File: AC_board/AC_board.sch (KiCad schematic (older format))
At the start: 10 parts, among them J1 1226, J2 7471287, J3 Conn_01x02_Male, J4 7471287, J5 7471287, J6 Conn_01x02_Male, K1 G6B-2214P-US-DC12

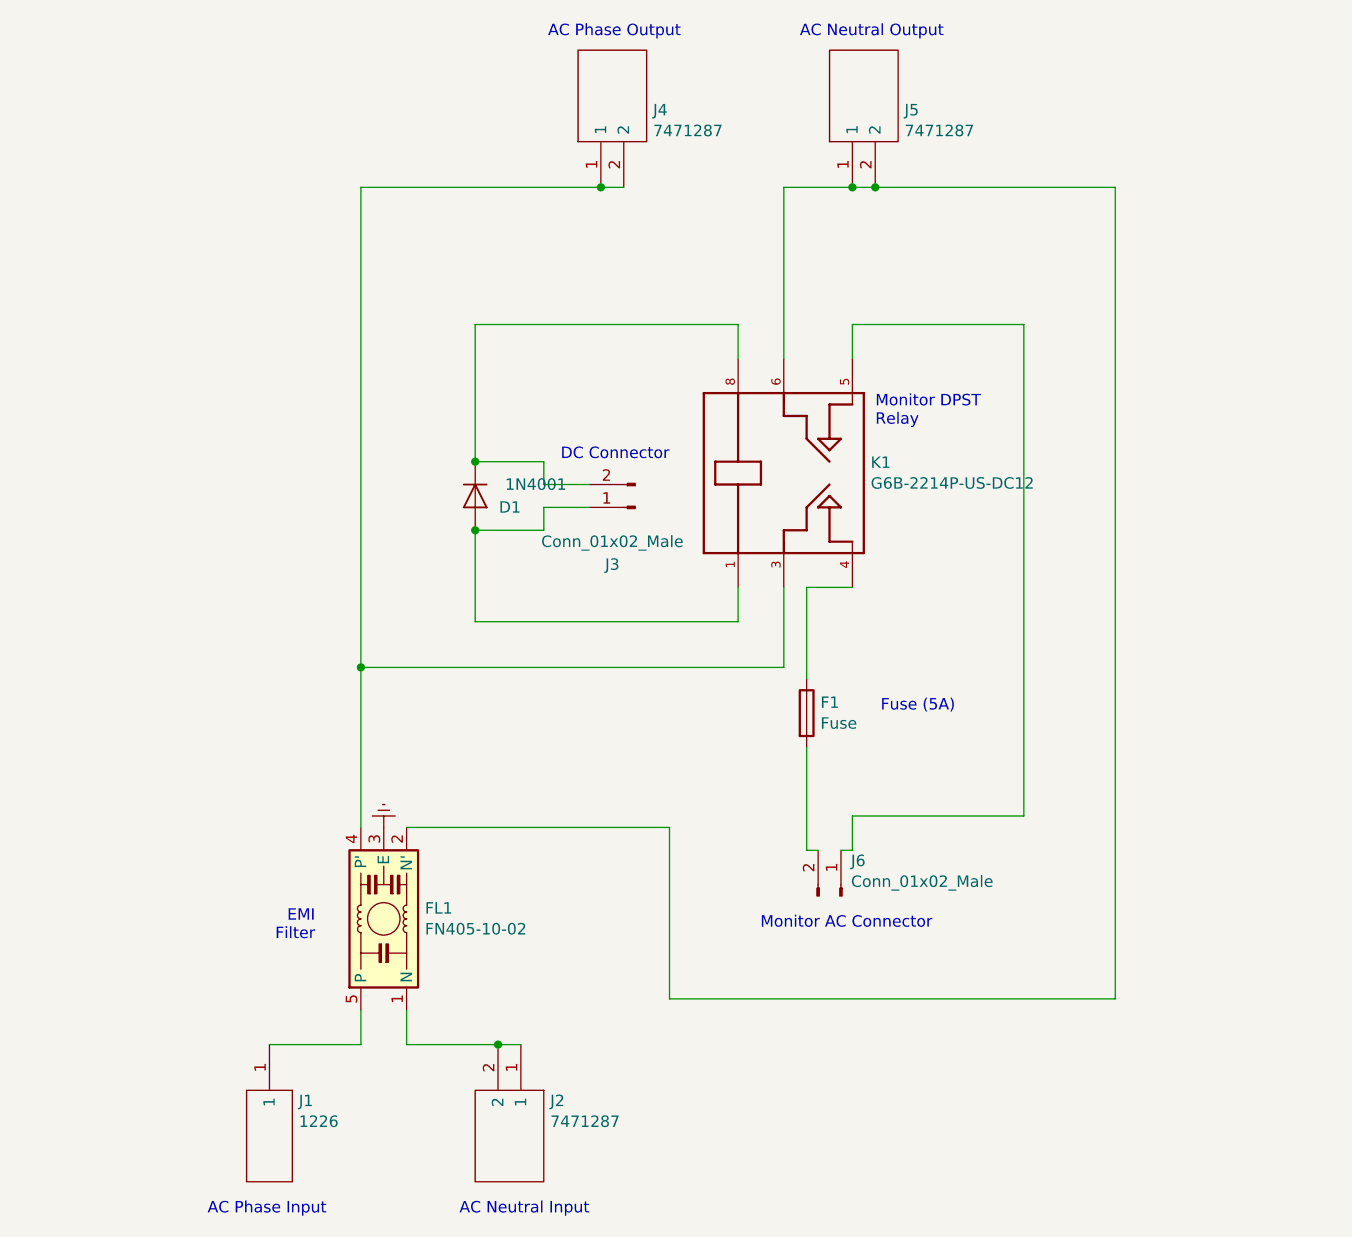
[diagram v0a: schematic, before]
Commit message: Brand new AC and DC boards
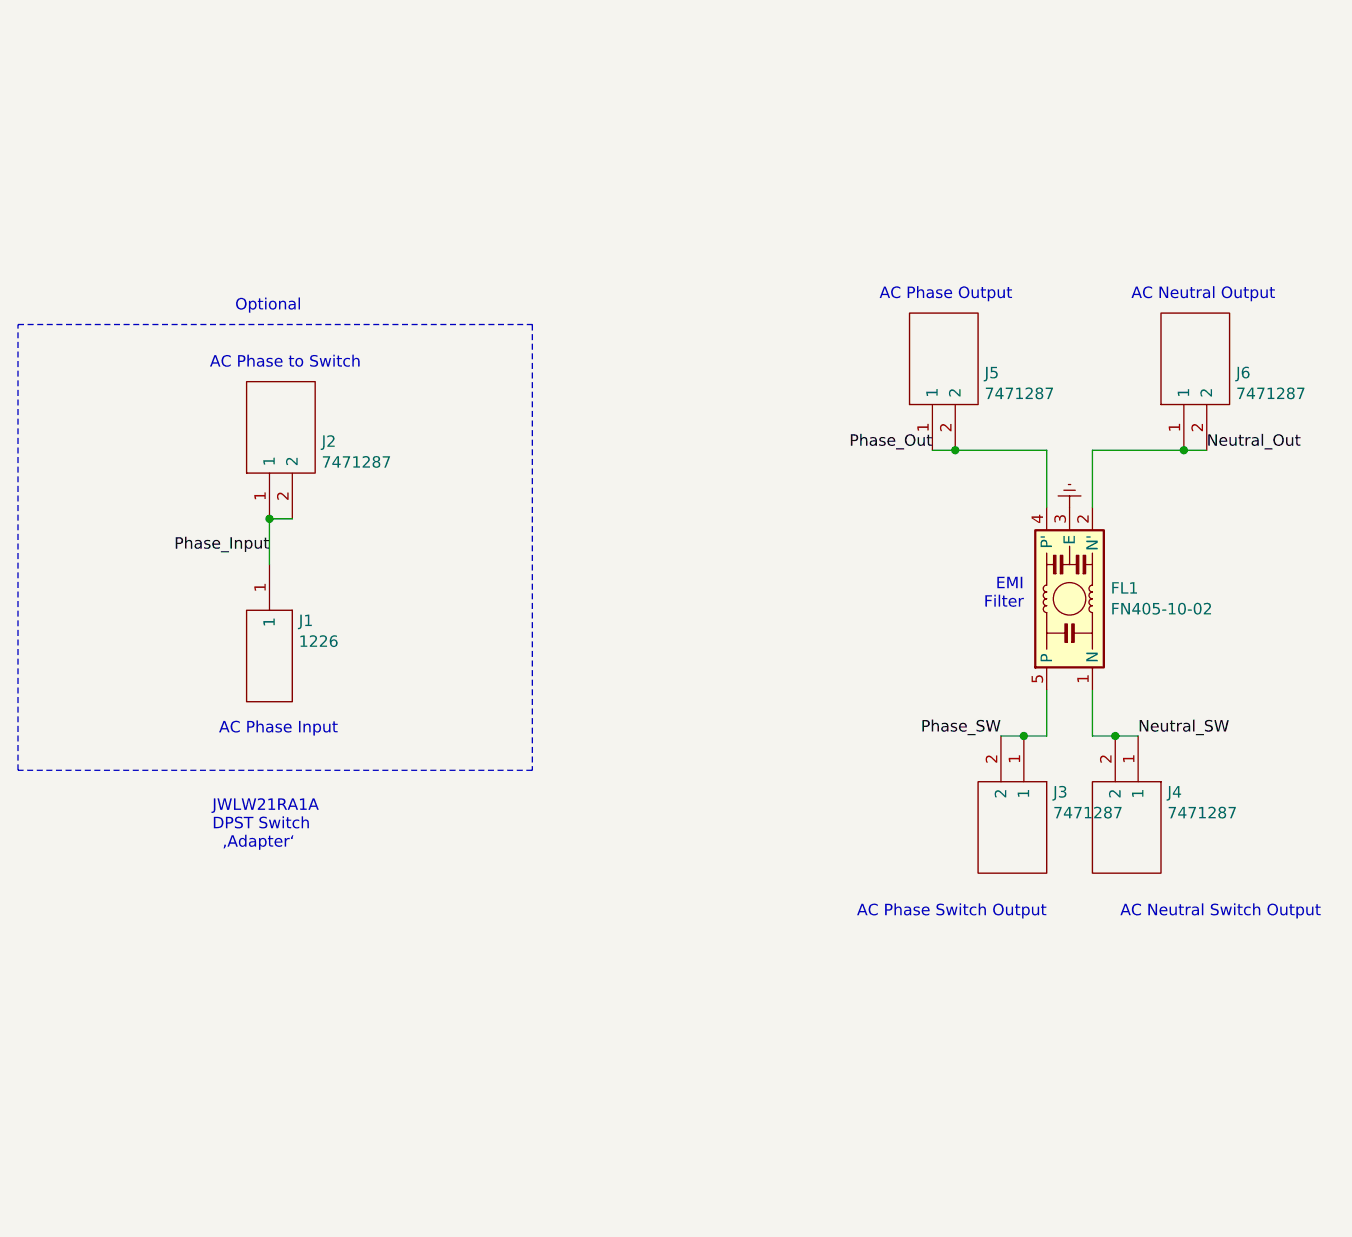
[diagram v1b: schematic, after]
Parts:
- removed D1: 1N4001, Diode_THT:D_DO-41_SOD81_P10.16mm_Horizontal, symbol Diode:1N4001
- removed F1: Fuse, Fuses_and_Holders_new:Fuseholder5x20_horiz_open_lateral_Type-II, symbol Device:Fuse
- removed J3: Conn_01x02_Male, Connector_Molex:Molex_KK-254_AE-6410-02A_1x02_P2.54mm_Vertical, symbol Connector:Conn_01x02_Male
- removed J6: Conn_01x02_Male, Monitor_Out:Molex_KK-396_2_pin_large, symbol Connector:Conn_01x02_Male
- removed K1: G6B-2214P-US-DC12, Omron_Relay:OM_G6B-2214P-US-DC24, symbol Omron_Relay:G6B-2214P-US-DC24
- added J2, J3: 7471287, Spade_large:7471287_large, symbol Spade_ATX_Quadra:7471287
- renumbered J2 to J4, J4 to J5, J5 to J6
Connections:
- net Phase_Input: now reaches J1.1
- net Phase_Input: now also J2.1, J2.2; no longer FL1.5 (P)
- net Neutral_SW: now reaches FL1.1 (N), J4.1, J4.2
- net Neutral_Out: now reaches FL1.2 (N'), J6.1, J6.2
- net Phase_Out: now reaches FL1.4 (P'), J5.1, J5.2
- new net Phase_SW: FL1.5 (P), J3.1, J3.2
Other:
- note added: "AC Neutral Switch Output"
- note added: "AC Phase Switch Output"
- note added: "AC Phase to Switch"
- note added: "JWLW21RA1A\nDPST Switch\n ‚Adapter‘"
- note added: "Optional"
- note removed: "AC Neutral Input"
- note removed: "DC Connector"
- note removed: "Fuse (5A)"
- note removed: "Monitor AC Connector"
- note removed: "Monitor DPST\nRelay"
- moved on the sheet: FL1, J1, J4, J5, J6
